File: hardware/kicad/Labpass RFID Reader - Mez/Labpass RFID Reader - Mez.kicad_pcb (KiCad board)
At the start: 2 copper layers, 61 x 70.1 mm, 15 parts, among them J1 Conn_01x03_Male

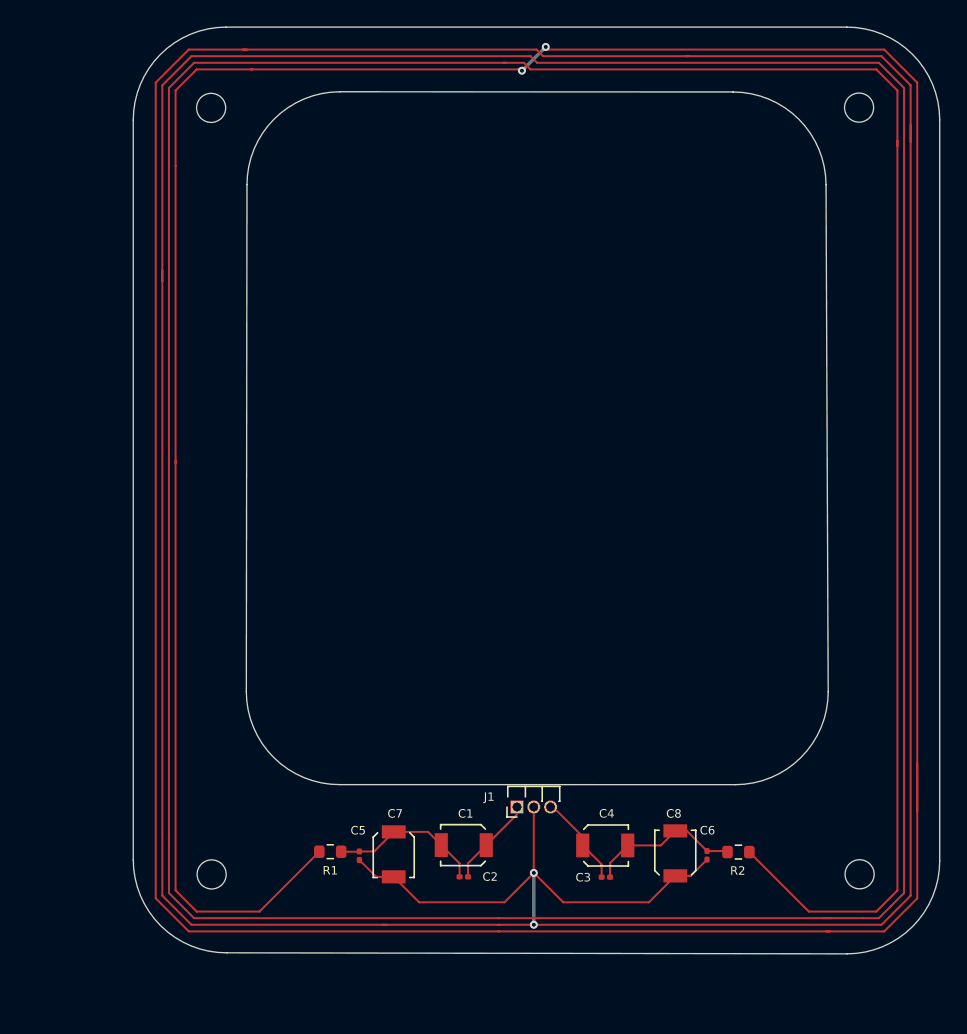
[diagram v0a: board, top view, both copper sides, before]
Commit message: Polish reposition pin headers to clear mez board
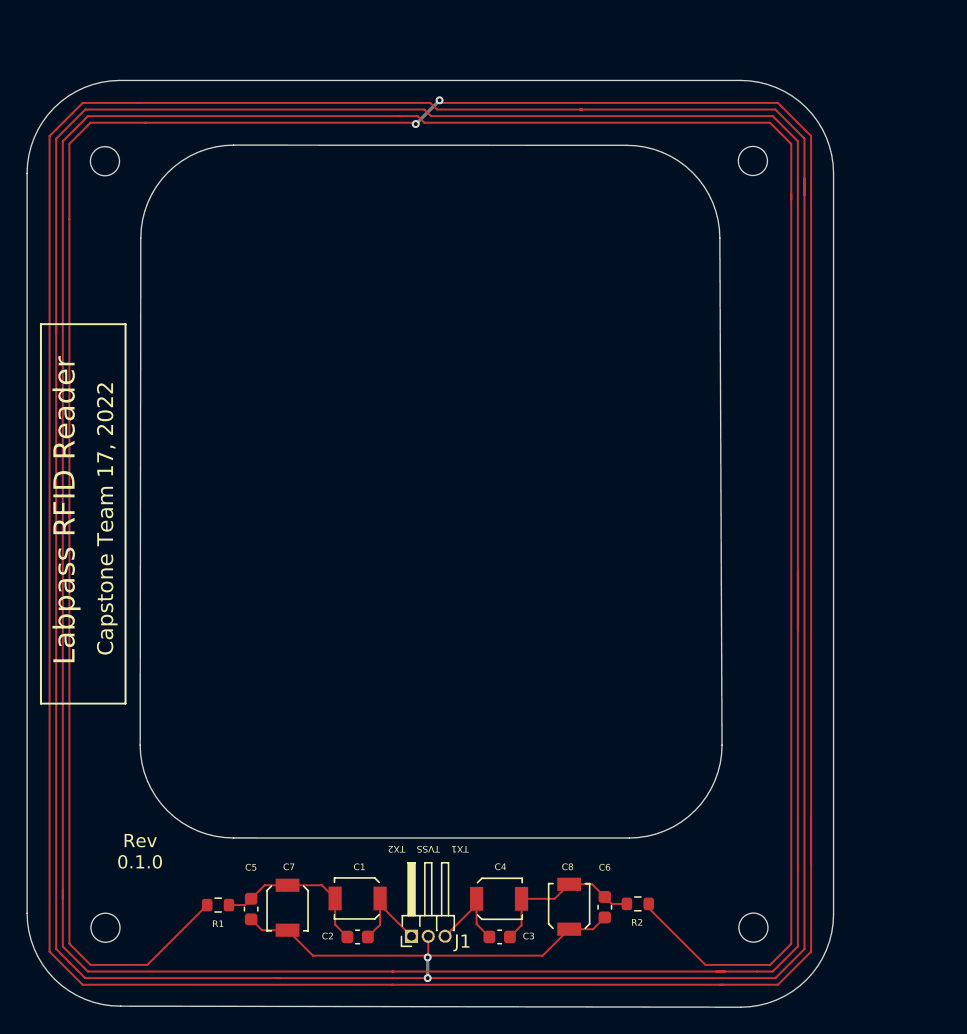
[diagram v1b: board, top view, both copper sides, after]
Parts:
- C2, C3, C5, C6: footprint Capacitor_SMD:C_0201_0603Metric -> Capacitor_SMD:C_0603_1608Metric
- J1: footprint Capstone Footprint Library:PinHeader_1x03_P1.27mm_Horizontal -> Connector_PinHeader_1.27mm:PinHeader_1x03_P1.27mm_Horizontal
- moved J1 12.6 mm to (138.1, 119.2)
- moved R1 9.39 mm to (123.5, 116.9)
- moved C2 9.23 mm to (134.0, 119.3)
- moved C3 9.21 mm to (144.8, 119.3)
- moved C5 9.12 mm to (126.0, 117.2)
- moved C4 8.99 mm to (144.7, 116.4)
- moved C7 8.99 mm to (128.7, 117.1)
- moved REF** 8.99 mm to (114.9, 60.6)
- moved REF** 8.99 mm to (115.0, 118.6)
- moved C1 8.99 mm to (134.0, 116.4)
- moved C8 8.99 mm to (150.0, 117.0)
- moved REF** 8.99 mm to (163.9, 60.6)
- moved REF** 8.99 mm to (164.0, 118.6)
- moved C6 8.67 mm to (152.7, 117.0)
- moved R2 8.56 mm to (155.2, 116.8)
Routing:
- net Net-(C5-Pad1): track 977.6 -> 969.4 mm
- net Net-(C1-Pad2): track 11.6 -> 12.4 mm
- net Net-(C3-Pad2): track 11.6 -> 12.3 mm
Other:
- board text added: "Capstone Team 17, 2022"
- board text added: "Labpass RFID Reader"
- board text added: "Rev 0.1.0"
- board text added: "TVSS"
- board text added: "TX1"
- board text added: "TX2"

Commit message: last-minute fixes
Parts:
- J1: footprint Connector_PinHeader_1.27mm:PinHeader_1x03_P1.27mm_Horizontal -> Capstone Footprint Library:PinHeader_1x03_P2.54mm_Horizontal
- moved J1 3.18 mm to (136.7, 116.4)
- moved C1 1.92 mm to (132.1, 116.4)
- moved C2 1.92 mm to (132.1, 119.3)
- moved C5 1.92 mm to (124.0, 117.2)
- moved C7 1.92 mm to (126.8, 117.1)
- moved R1 1.92 mm to (121.5, 116.9)
- moved C4 1.58 mm to (146.3, 116.4)
- moved C6 1.58 mm to (154.3, 117.0)
- moved R2 1.58 mm to (156.8, 116.8)
- moved C3 1.58 mm to (146.3, 119.3)
- moved C8 1.58 mm to (151.6, 117.0)
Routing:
- net Net-(C5-Pad1): track 969.4 -> 972.2 mm
- net Net-(C1-Pad1): track 7.14 -> 6.16 mm
- net Net-(C3-Pad1): track 7.11 -> 6.15 mm
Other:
- rule pad_to_mask_clearance: 0 -> 0.0508

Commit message: kicad backups
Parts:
- C1, C4, C7, C8: value C -> 8-40p
- C2, C3: value C -> NC
- C5, C6: value C -> 30p
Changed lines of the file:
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@@
       (effects (font (size 0.5 0.5) (thickness 0.15)))
     )
-    (fp_text value "C" (at 1.614 2.4064) (layer "F.Fab") hide
-      (effects (font (size 0.64 0.64) (thickness 0.15)))
+    (fp_text value "8-40p" (at 0.02 3.091005) (layer "F.Fab")
+      (effects (font (size 1 1) (thickness 0.15)))
     )
     (fp_line (start 1.75 1.55) (end -1.3 1.55) (layer "F.SilkS") (width 0.127))
@@
       (effects (font (size 0.5 0.5) (thickness 0.15)))
     )
-    (fp_text value "C" (at 0 1.43 90) (layer "F.Fab") hide
+    (fp_text value "30p" (at -2.204995 -1.110907 180) (layer "F.Fab")
       (effects (font (size 1 1) (thickness 0.15)))
     )
@@
       (effects (font (size 0.5 0.5) (thickness 0.15)))
     )
-    (fp_text value "C" (at 0 1.43 180) (layer "F.Fab") hide
+    (fp_text value "NC" (at 0 -2.127001 180) (layer "F.Fab")
       (effects (font (size 1 1) (thickness 0.15)))
     )
@@
       (effects (font (size 0.5 0.5) (thickness 0.15)))
     )
-    (fp_text value "C" (at 1.614 2.4064 90) (layer "F.Fab")
-      (effects (font (size 0.64 0.64) (thickness 0.15)))
+    (fp_text value "8-40p" (at -4.412 -0.216 180) (layer "F.Fab")
+      (effects (font (size 1 1) (thickness 0.15)))
     )
     (fp_line (start -1.632 -1.219) (end -1.3 -1.55) (layer "F.SilkS") (width 0.127))
@@
       (effects (font (size 0.5 0.5) (thickness 0.15)))
     )
-    (fp_text value "R_US" (at 0 1.43) (layer "F.Fab") hide
-      (effects (font (size 1 1) (thickness 0.15)))
-    )
-    (fp_text user "${REFERENCE}" (at 0 0) (layer "F.Fab")
+    (fp_text value "R_US" (at 0.175093 -1.976994) (layer "F.Fab")
+      (effects (font (size 1 1) (thickness 0.15)))
+    )
+    (fp_text user "${REFERENCE}" (at 0 0) (layer "F.Fab") hide
       (effects (font (size 0.5 0.5) (thickness 0.06)))
     )
@@
       (effects (font (size 0.5 0.5) (thickness 0.15)))
     )
-    (fp_text value "C" (at 1.614 2.4064) (layer "F.Fab")
-      (effects (font (size 0.64 0.64) (thickness 0.15)))
+    (fp_text value "8-40p" (at 0.004 -3.116) (layer "F.Fab")
+      (effects (font (size 1 1) (thickness 0.15)))
     )
     (fp_line (start 1.75 1.55) (end 1.75 1.22) (layer "F.SilkS") (width 0.127))
@@
       (effects (font (size 0.5 0.5) (thickness 0.15)))
     )
-    (fp_text value "C" (at 0 1.43) (layer "F.Fab") hide
-      (effects (font (size 1 1) (thickness 0.15)))
-    )
-    (fp_text user "${REFERENCE}" (at 0 0) (layer "F.Fab")
+    (fp_text value "NC" (at 0 2.127006) (layer "F.Fab")
+      (effects (font (size 1 1) (thickness 0.15)))
+    )
+    (fp_text user "${REFERENCE}" (at 0 2.635006) (layer "F.Fab") hide
       (effects (font (size 0.5 0.5) (thickness 0.06)))
     )
@@
       (effects (font (size 0.5 0.5) (thickness 0.15)))
     )
-    (fp_text value "R_US" (at 0 1.43) (layer "F.Fab") hide
-      (effects (font (size 1 1) (thickness 0.15)))
-    )
-    (fp_text user "${REFERENCE}" (at 0 0) (layer "F.Fab")
+    (fp_text value "R_US" (at 0 2.067005) (layer "F.Fab")
+      (effects (font (size 1 1) (thickness 0.15)))
+    )
+    (fp_text user "${REFERENCE}" (at 0 0) (layer "F.Fab") hide
       (effects (font (size 0.5 0.5) (thickness 0.06)))
     )
@@
       (effects (font (size 0.5 0.5) (thickness 0.15)))
     )
-    (fp_text value "C" (at 1.614 2.4064 90) (layer "F.Fab") hide
-      (effects (font (size 0.64 0.64) (thickness 0.15)))
+    (fp_text value "8-40p" (at 4.336995 -0.2 180) (layer "F.Fab")
+      (effects (font (size 1 1) (thickness 0.15)))
     )
     (fp_line (start -1.3 -1.55) (end 1.75 -1.55) (layer "F.SilkS") (width 0.127))
@@
       (effects (font (size 0.5 0.5) (thickness 0.15)))
     )
-    (fp_text value "C" (at 0 1.43 -90) (layer "F.Fab") hide
-      (effects (font (size 1 1) (thickness 0.15)))
-    )
-    (fp_text user "${REFERENCE}" (at 0 0 -90) (layer "F.Fab")
-      (effects (font (size 0.5 0.5) (thickness 0.06)))
-    )
+    (fp_text value "30p" (at 2.345006 -1.151093) (layer "F.Fab")
+      (effects (font (size 1 1) (thickness 0.15)))
+    )
+    (fp_text user "${REFERENCE}" (at -2.226994 0) (layer "F.Fab") hide
+      (effects (font (size 0.5 0.5) (thickness 0.06)))
+    )

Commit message: temp
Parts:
- C1: footprint Capstone Footprint Library:JR400 -> Resistor_SMD:R_0603_1608Metric
- C4, C7, C8: footprint Capstone Footprint Library:JR400 -> Capacitor_SMD:C_0603_1608Metric
- REF** (x4): value MountingHole_2.2mm_M2_ISO14580 -> MountingHole_2.5mm; footprint MountingHole:MountingHole_2.2mm_M2_ISO14580 -> MountingHole:MountingHole_2.5mm
- moved C2 1.43 mm to (132.1, 117.9)
- moved C3 1.17 mm to (146.3, 118.1)
- moved C7 1.07 mm to (125.7, 117.1)
- moved C8 1.06 mm to (152.7, 117.1)
- moved R1 0.54 mm to (121.5, 116.3)
- moved R2 0.45 mm to (156.8, 116.3)
- moved C6 0.07 mm to (154.3, 117.1)
- moved C5 0.07 mm to (124.0, 117.1)
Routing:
- net Net-(C1-Pad2): track 12.4 -> 10.4 mm
- net Net-(C3-Pad2): track 12.3 -> 10.6 mm
- net Net-(C1-Pad1): track 6.16 -> 5.25 mm
- net Net-(C3-Pad1): track 6.15 -> 5.45 mm
- net Net-(C5-Pad1): track 972.2 -> 972.8 mm
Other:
- board text added: "Rev 1.0.0"
- board text removed: "Rev 0.1.0"

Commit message: bump rev to 1.0.0
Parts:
- removed REF** (x4): MountingHole_2.5mm, MountingHole:MountingHole_2.5mm
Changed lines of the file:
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@@
   (title_block
     (title "Labpass RFID Reader - Mezzanine")
-    (date "2022-05-10")
+    (date "2022-05-15")
     (rev "1.0.0")
   )
@@
     )
   )
-  (footprint "MountingHole:MountingHole_2.5mm" (layer "F.Cu")
-    (at 163.923097 60.590005)
-    (descr "Mounting Hole 2.5mm, no annular")
-    (tags "mounting hole 2.5mm no annular")
-    (attr exclude_from_pos_files exclude_from_bom)
-    (fp_text reference "REF**" (at 0 -3.5) (layer "F.SilkS") hide
-      (effects (font (size 1 1) (thickness 0.15)))
-    )
-    (fp_text value "MountingHole_2.5mm" (at 0 3.5) (layer "F.Fab") hide
-      (effects (font (size 1 1) (thickness 0.15)))
-    )
-    (fp_text user "${REFERENCE}" (at 0 0) (layer "F.Fab") hide
-      (effects (font (size 1 1) (thickness 0.15)))
-    )
-    (fp_circle (center 0 0) (end 2.5 0) (layer "Cmts.User") (width 0.15) (fill none))
-    (fp_circle (center 0 0) (end 2.75 0) (layer "F.CrtYd") (width 0.05) (fill none))
-    (pad "" np_thru_hole circle (at 0 0) (size 2.5 2.5) (drill 2.5) (layers *.Cu *.Mask))
-  )
-  (footprint "MountingHole:MountingHole_2.5mm" (layer "F.Cu")
-    (at 163.963097 118.580005)
-    (descr "Mounting Hole 2.5mm, no annular")
-    (tags "mounting hole 2.5mm no annular")
-    (attr exclude_from_pos_files exclude_from_bom)
-    (fp_text reference "REF**" (at 0 -3.5) (layer "F.SilkS") hide
-      (effects (font (size 1 1) (thickness 0.15)))
-    )
-    (fp_text value "MountingHole_2.5mm" (at 0 3.5) (layer "F.Fab") hide
-      (effects (font (size 1 1) (thickness 0.15)))
-    )
-    (fp_text user "${REFERENCE}" (at 0 0) (layer "F.Fab") hide
-      (effects (font (size 1 1) (thickness 0.15)))
-    )
-    (fp_circle (center 0 0) (end 2.5 0) (layer "Cmts.User") (width 0.15) (fill none))
-    (fp_circle (center 0 0) (end 2.75 0) (layer "F.CrtYd") (width 0.05) (fill none))
-    (pad "" np_thru_hole circle (at 0 0) (size 2.5 2.5) (drill 2.5) (layers *.Cu *.Mask))
-  )
   (footprint "Capacitor_SMD:C_0603_1608Metric" (layer "F.Cu")
     (at 132.1 117.856 180)
@@
       (rotate (xyz 0 0 0))
     )
-  )
-  (footprint "MountingHole:MountingHole_2.5mm" (layer "F.Cu")
-    (at 114.953097 118.590005)
-    (descr "Mounting Hole 2.5mm, no annular")
-    (tags "mounting hole 2.5mm no annular")
-    (attr exclude_from_pos_files exclude_from_bom)
-    (fp_text reference "REF**" (at 0 -3.5) (layer "F.SilkS") hide
-      (effects (font (size 1 1) (thickness 0.15)))
-    )
-    (fp_text value "MountingHole_2.5mm" (at 0 3.5) (layer "F.Fab") hide
-      (effects (font (size 1 1) (thickness 0.15)))
-    )
-    (fp_text user "${REFERENCE}" (at 0 0) (layer "F.Fab") hide
-      (effects (font (size 1 1) (thickness 0.15)))
-    )
-    (fp_circle (center 0 0) (end 2.5 0) (layer "Cmts.User") (width 0.15) (fill none))
-    (fp_circle (center 0 0) (end 2.75 0) (layer "F.CrtYd") (width 0.05) (fill none))
-    (pad "" np_thru_hole circle (at 0 0) (size 2.5 2.5) (drill 2.5) (layers *.Cu *.Mask))
-  )
-  (footprint "MountingHole:MountingHole_2.5mm" (layer "F.Cu")
-    (at 114.913097 60.610005)
-    (descr "Mounting Hole 2.5mm, no annular")
-    (tags "mounting hole 2.5mm no annular")
-    (attr exclude_from_pos_files exclude_from_bom)
-    (fp_text reference "REF**" (at 0 -3.5) (layer "F.SilkS") hide
-      (effects (font (size 1 1) (thickness 0.15)))
-    )
-    (fp_text value "MountingHole_2.5mm" (at 0 3.5) (layer "F.Fab") hide
-      (effects (font (size 1 1) (thickness 0.15)))
-    )
-    (fp_text user "${REFERENCE}" (at 0 0) (layer "F.Fab") hide
-      (effects (font (size 1 1) (thickness 0.15)))
-    )
-    (fp_circle (center 0 0) (end 2.5 0) (layer "Cmts.User") (width 0.15) (fill none))
-    (fp_circle (center 0 0) (end 2.75 0) (layer "F.CrtYd") (width 0.05) (fill none))
-    (pad "" np_thru_hole circle (at 0 0) (size 2.5 2.5) (drill 2.5) (layers *.Cu *.Mask))
   )
   (footprint "Resistor_SMD:R_0603_1608Metric" (layer "F.Cu")
@@
   (segment (start 150.823097 56.700005) (end 165.623097 56.700005) (width 0.1524) (layer "F.Cu") (net 5))
   (segment (start 168.323097 120.400005) (end 165.823097 122.900005) (width 0.1524) (layer "F.Cu") (net 5))
-  (segment (start 112.223097 119.800005) (end 112.223097 87.300005) (width 0.1524) (layer "F.Cu") (net 5))
   (segment (start 136.906 120.904) (end 128.498 120.904) (width 0.25) (layer "F.Cu") (net 5))
+  (segment (start 116.196907 121.400005) (end 113.823097 121.400005) (width 0.1524) (layer "F.Cu") (net 5))
   (segment (start 110.723097 58.700005) (end 113.223097 56.200005) (width 0.1524) (layer "F.Cu") (net 5))
   (segment (start 113.623097 121.900005) (end 111.723097 120.000005) (width 0.1524) (layer "F.Cu") (net 5))
+  (segment (start 113.823097 121.400005) (end 112.223097 119.800005) (width 0.1524) (layer "F.Cu") (net 5))
   (segment (start 111.223097 120.200005) (end 111.223097 72.900005) (width 0.1524) (layer "F.Cu") (net 5))
-  (segment (start 113.823097 121.400005) (end 112.223097 119.800005) (width 0.1524) (layer "F.Cu") (net 5))
   (segment (start 139.073097 57.700005) (end 165.223097 57.700005) (width 0.1524) (layer "F.Cu") (net 5))
   (segment (start 167.823097 58.900005) (end 167.823097 63.200005) (width 0.1524) (layer "F.Cu") (net 5))
@@
   (segment (start 137.023097 57.200005) (end 138.573097 57.200005) (width 0.1524) (layer "F.Cu") (net 5))
   (segment (start 167.823097 120.200005) (end 165.623097 122.400005) (width 0.1524) (layer "F.Cu") (net 5))
-  (segment (start 116.196907 121.400005) (end 113.823097 121.400005) (width 0.1524) (layer "F.Cu") (net 5))
   (segment (start 113.423097 122.400005) (end 111.223097 120.200005) (width 0.1524) (layer "F.Cu") (net 5))
   (segment (start 112.223097 87.500005) (end 112.223097 65.000005) (width 0.1524) (layer "F.Cu") (net 5))
@@
   (segment (start 140.023097 56.700005) (end 151.023097 56.700005) (width 0.1524) (layer "F.Cu") (net 5))
   (segment (start 136.723097 122.400005) (end 127.823097 122.400005) (width 0.1524) (layer "F.Cu") (net 5))
+  (segment (start 120.721907 116.332) (end 120.721907 116.875005) (width 0.1524) (layer "F.Cu") (net 5))
   (segment (start 166.823097 63.100005) (end 166.823097 119.800005) (width 0.1524) (layer "F.Cu") (net 5))
   (segment (start 166.823097 59.300005) (end 166.823097 63.500005) (width 0.1524) (layer "F.Cu") (net 5))
@@
   (segment (start 139.2 116.4) (end 139.2 120.834999) (width 0.25) (layer "F.Cu") (net 5))
   (segment (start 154.296907 117.882) (end 152.654 117.882) (width 0.25) (layer "F.Cu") (net 5))
-  (segment (start 120.721907 116.875005) (end 116.196907 121.400005) (width 0.1524) (layer "F.Cu") (net 5))
   (segment (start 110.723097 120.400005) (end 110.723097 58.700005) (width 0.1524) (layer "F.Cu") (net 5))
   (segment (start 161.823097 121.900005) (end 136.623097 121.900005) (width 0.1524) (layer "F.Cu") (net 5))
@@
   (segment (start 112.223097 59.300005) (end 113.623097 57.900005) (width 0.1524) (layer "F.Cu") (net 5))
   (segment (start 168.323097 110.200005) (end 168.323097 120.400005) (width 0.1524) (layer "F.Cu") (net 5))
+  (segment (start 112.223097 119.800005) (end 112.223097 87.300005) (width 0.1524) (layer "F.Cu") (net 5))
   (segment (start 165.823097 56.200005) (end 140.423097 56.200005) (width 0.1524) (layer "F.Cu") (net 5))
-  (segment (start 141.494 120.904) (end 141.732 120.904) (width 0.25) (layer "F.Cu") (net 5))
   (segment (start 138.573097 57.200005) (end 139.073097 57.700005) (width 0.1524) (layer "F.Cu") (net 5))
   (segment (start 139.073097 56.700005) (end 139.573097 57.200005) (width 0.1524) (layer "F.Cu") (net 5))
+  (segment (start 120.721907 116.875005) (end 116.196907 121.400005) (width 0.1524) (layer "F.Cu") (net 5))
   (segment (start 111.223097 58.900005) (end 113.423097 56.700005) (width 0.1524) (layer "F.Cu") (net 5))
   (segment (start 165.823097 122.900005) (end 161.423097 122.900005) (width 0.1524) (layer "F.Cu") (net 5))
